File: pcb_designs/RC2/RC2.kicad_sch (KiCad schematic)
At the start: 34 parts, among them J1 Screw_Terminal_01x02, J2 Conn_01x01_Socket, J3 Conn_01x01_Socket, J5 Screw_Terminal_01x02, J6 Conn_01x01_Socket, J7 Conn_01x01_Socket, J8 Conn_01x06_Pin, T1 CS1200L, T2 CS1200L, U1 LM339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

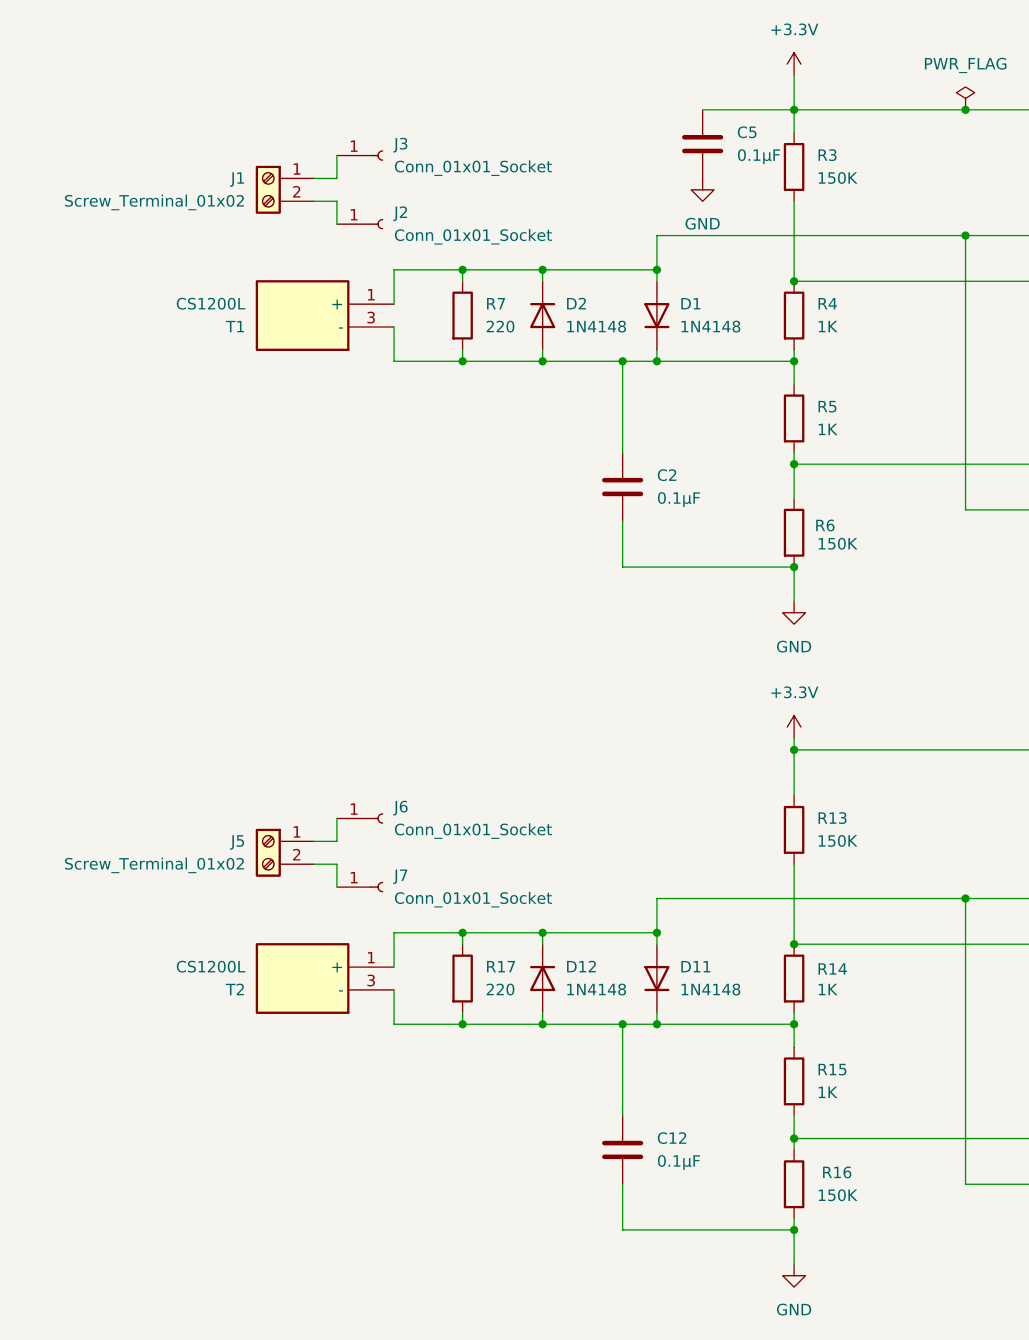
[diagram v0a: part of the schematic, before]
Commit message: Updated Schematic
Up date to the dual detector schematic.  N.B PCB layout to follow.

Plus a few cosmetic code changes.
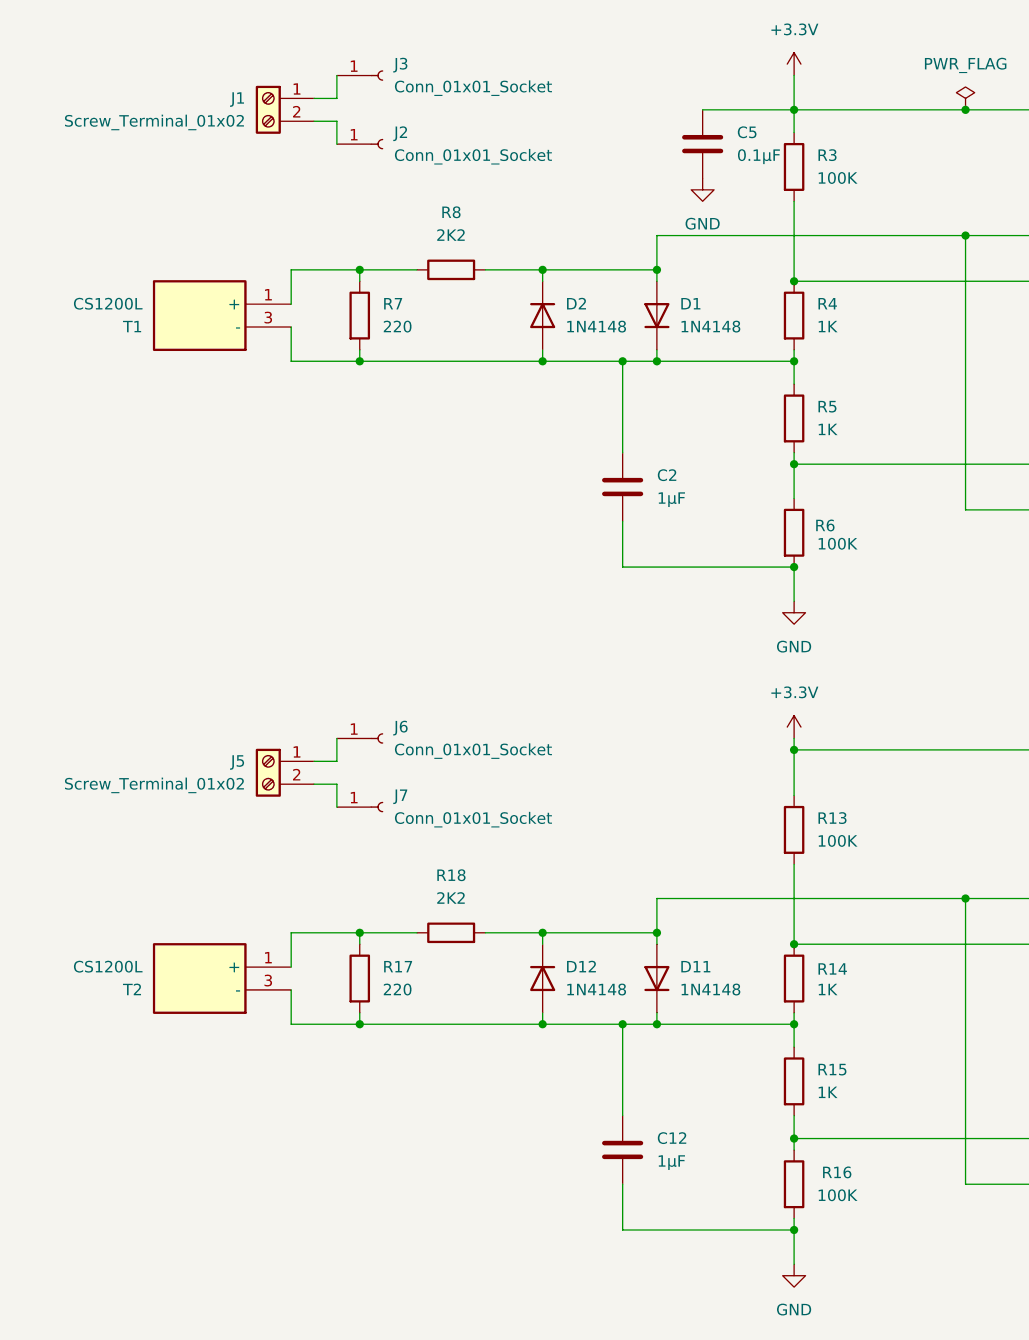
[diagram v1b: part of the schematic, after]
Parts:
- added R18, R8: 2K2, Resistor_THT:R_Axial_DIN0207_L6.3mm_D2.5mm_P7.62mm_Horizontal, symbol Device:R
- C12, C2: value 0.1µF -> 1µF
- R13, R16, R3, R6: value 150K -> 100K
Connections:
- net at D11.2 (A), D12.1 (K), U1.7 (+)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: now also R18.2; no longer R17.1, T2.1 (+)
- net at D1.2 (A), D2.1 (K), U1.10 (-)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: now also R8.2; no longer R7.1, T1.1 (+)
- new net: R7.1, R8.1, T1.1 (+)
- new net: R17.1, R18.1, T2.1 (+)
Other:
- moved on the sheet: J1, J2, J3, J5, J6, J7, R17, R7, T1, T2
